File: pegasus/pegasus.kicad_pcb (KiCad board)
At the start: 2 copper layers, 50 x 120 mm, 15 parts, among them IC1 RFD900, IC2 Adafruit, IC3 Adafruit-BNO055-PCB, IC4 L70B-M39, IC5 L7805ACV, J1 Conn_01x02_Female, J2 Conn_01x02_Female, U1 Teensy4.1, U2 CON-SMA-EDGE-S, U3 CON-SMA-EDGE-S

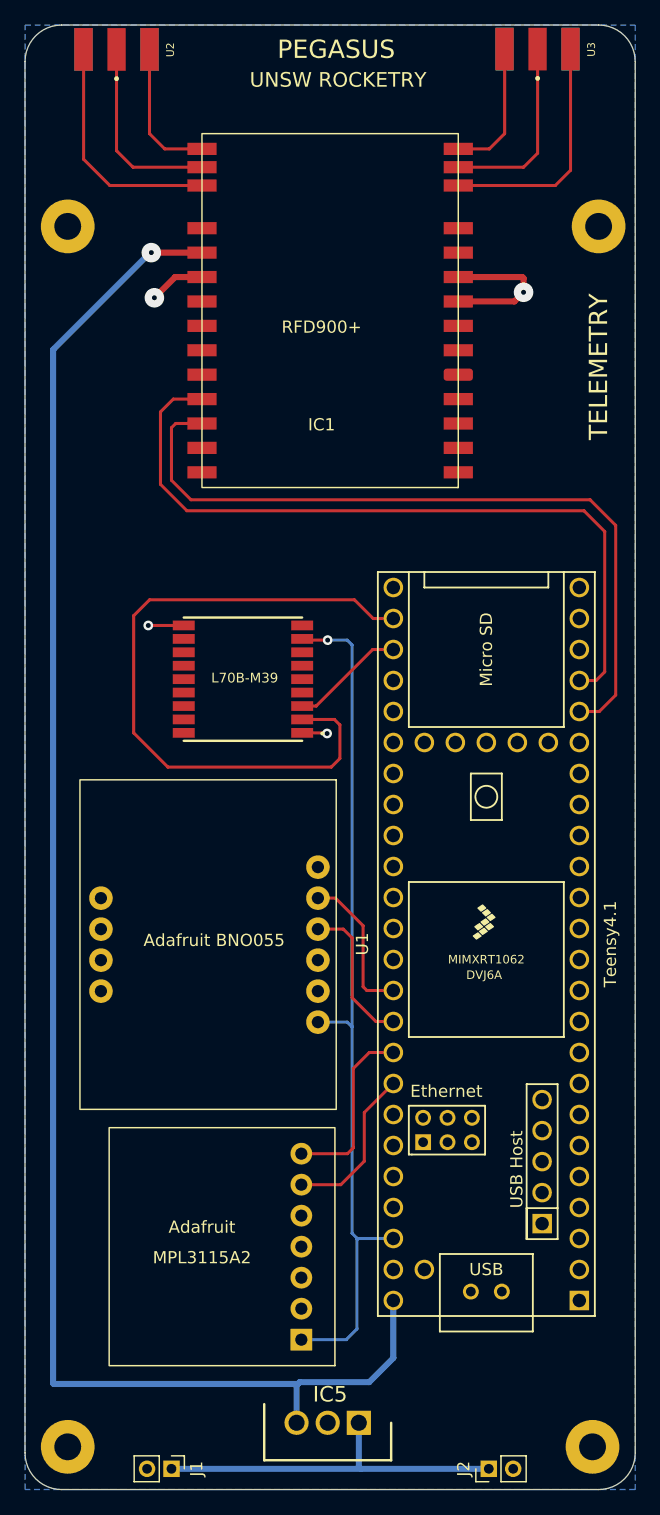
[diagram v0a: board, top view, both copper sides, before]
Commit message: added no connection flag to schematics, fixed minor mistakes on PCB and in footprints
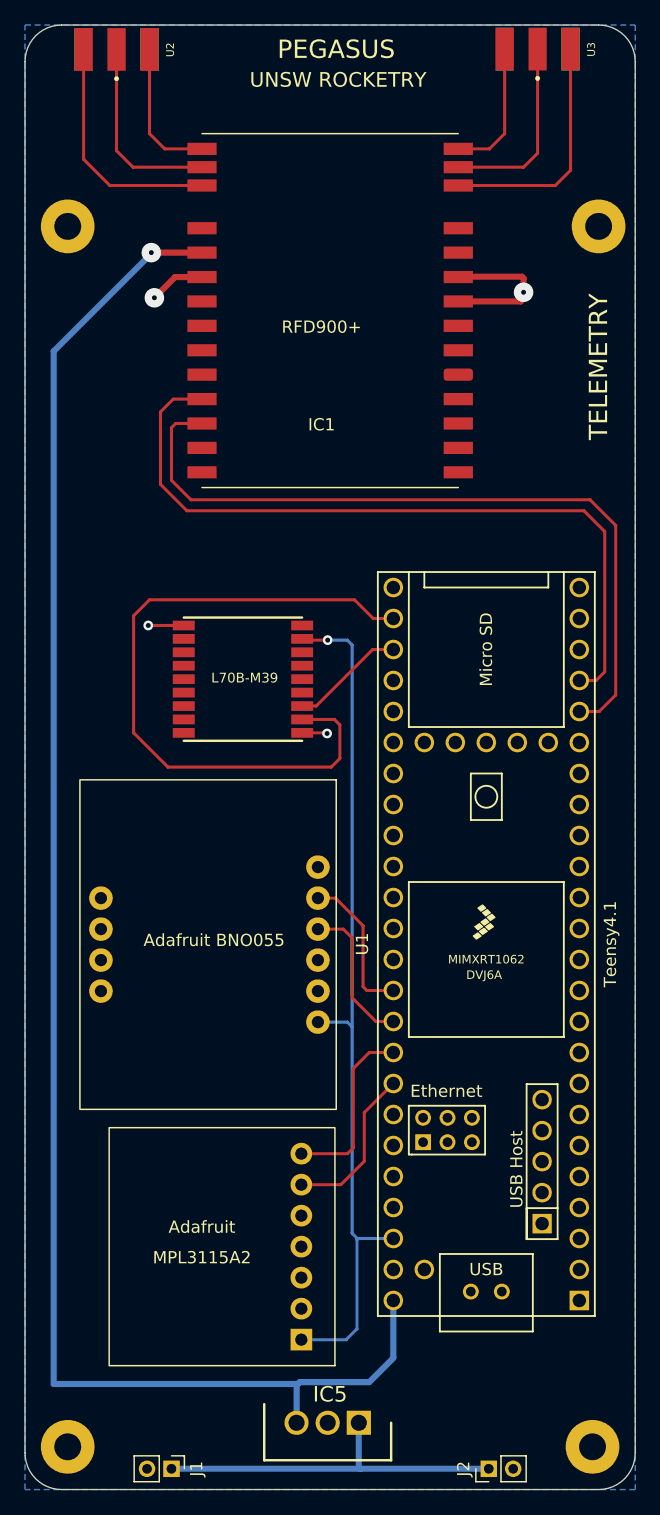
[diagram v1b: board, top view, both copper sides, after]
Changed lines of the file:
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@@
       (effects (font (size 1.27 1.27) (thickness 0.254)))
     )
-    (fp_line (start -4.85 -5.05) (end 4.85 -5.05) (layer "F.SilkS") (width 0.2))
     (fp_line (start 4.85 5.05) (end -4.85 5.05) (layer "F.SilkS") (width 0.2))
-    (fp_circle (center -6.502 -4.45) (end -6.502 -4.388) (layer "F.SilkS") (width 0.2) (fill none))
-    (fp_line (start -4.85 5.05) (end -4.85 -5.05) (layer "F.Fab") (width 0.2))
+    (fp_line (start -4.85 -5.05) (end 4.85 -5.05) (layer "F.SilkS") (width 0.2))
     (fp_line (start 4.85 -5.05) (end 4.85 5.05) (layer "F.Fab") (width 0.2))
-    (fp_line (start -4.85 -5.05) (end 4.85 -5.05) (layer "F.Fab") (width 0.2))
     (fp_line (start 4.85 5.05) (end -4.85 5.05) (layer "F.Fab") (width 0.2))
+    (fp_line (start -4.85 5.05) (end -4.85 -5.05) (layer "F.Fab") (width 0.2))
+    (fp_line (start -4.85 -5.05) (end 4.85 -5.05) (layer "F.Fab") (width 0.2))
     (pad "1" smd rect (at -4.85 -4.4 270) (size 0.8 1.8) (layers "F.Cu" "F.Paste" "F.Mask")
       (net 2 "GND") (pinfunction "GND_1") (pintype "passive"))
@@
       (effects (font (size 1 1) (thickness 0.15)))
     )
-    (fp_rect (start -6 -11.25) (end 15 17.75) (layer "F.SilkS") (width 0.12) (fill none))
+    (fp_line (start -6 -11.25) (end 15 -11.25) (layer "F.SilkS") (width 0.12))
+    (fp_line (start 15 17.75) (end -6 17.75) (layer "F.SilkS") (width 0.12))
+    (fp_line (start 15 -11.25) (end 15 17.75) (layer "Dwgs.User") (width 0.12))
+    (fp_line (start -6 17.75) (end -6 -11.25) (layer "Dwgs.User") (width 0.12))
     (pad "1" smd rect (at -6 -10 180) (size 2.4 1) (layers "F.Cu" "F.Paste" "F.Mask")
       (net 1 "unconnected-(IC1-Pad1)") (pinfunction "VUSB_5V") (pintype "input"))
@@
     (pad "28" smd rect (at 15 -10 180) (size 2.4 1) (layers "F.Cu" "F.Paste" "F.Mask")
       (net 24 "unconnected-(IC1-Pad28)") (pinfunction "CTS") (pintype "input"))
-    (group "" (id 5d567197-105f-4ed3-a4d4-dfc5e32b2ccc)
+    (group "" (id ccf65e24-b980-469f-8862-e397985c8f5a)
       (members
-        1bda36f6-3944-4bdf-b224-5bfc97f22460
-        25f77a41-6639-47ca-88a6-aa38a4b331a1
-        93e5cccc-95f5-49e8-be9b-0aba27195b61
-        b404786f-6892-43d8-8cbe-df439968c1ea
-        da67685b-35ec-44e4-9884-b9158b872c0e
-        de8f9472-fcc7-403f-a0e1-fee3a16774bd
+        01478f52-711e-460d-9130-927d9df325cb
+        142e2cf6-b82f-4007-9894-377d26b8ab0d
+        28221cea-e5dd-4443-909d-f89dc42a5054
+        59fe4e68-4119-4952-b511-7d1576b16691
+        7bdee640-e6be-4899-b318-a0ad1af68164
+        d9a88a97-e7e1-4571-8028-07e1b736766b
       )
     )
@@
     (fp_line (start -7.62 -0.635) (end -7.62 0.635) (layer "F.Fab") (width 0.2032))
     (fp_poly (pts
+        (xy -4.064 0.254)
+        (xy -3.556 0.254)
+        (xy -3.556 -0.254)
+        (xy -4.064 -0.254)
+      ) (layer "F.Fab") (width 0) (fill solid))
+    (fp_poly (pts
         (xy 3.556 0.254)
         (xy 4.064 0.254)
@@
       ) (layer "F.Fab") (width 0) (fill solid))
     (fp_poly (pts
-        (xy 3.556 -17.526)
-        (xy 4.064 -17.526)
-        (xy 4.064 -18.034)
-        (xy 3.556 -18.034)
-      ) (layer "F.Fab") (width 0) (fill solid))
-    (fp_poly (pts
-        (xy -1.524 0.254)
-        (xy -1.016 0.254)
-        (xy -1.016 -0.254)
-        (xy -1.524 -0.254)
-      ) (layer "F.Fab") (width 0) (fill solid))
-    (fp_poly (pts
         (xy -4.064 -17.526)
         (xy -3.556 -17.526)
@@
       ) (layer "F.Fab") (width 0) (fill solid))
     (fp_poly (pts
+        (xy -1.524 0.254)
+        (xy -1.016 0.254)
+        (xy -1.016 -0.254)
+        (xy -1.524 -0.254)
+      ) (layer "F.Fab") (width 0) (fill solid))
+    (fp_poly (pts
+        (xy 3.556 -17.526)
+        (xy 4.064 -17.526)
+        (xy 4.064 -18.034)
+        (xy 3.556 -18.034)
+      ) (layer "F.Fab") (width 0) (fill solid))
+    (fp_poly (pts
         (xy -1.524 -17.526)
         (xy -1.016 -17.526)
@@
       ) (layer "F.Fab") (width 0) (fill solid))
     (fp_poly (pts
-        (xy 1.016 0.254)
-        (xy 1.524 0.254)
-        (xy 1.524 -0.254)
-        (xy 1.016 -0.254)
-      ) (layer "F.Fab") (width 0) (fill solid))
-    (fp_poly (pts
-        (xy -4.064 0.254)
-        (xy -3.556 0.254)
-        (xy -3.556 -0.254)
-        (xy -4.064 -0.254)
-      ) (layer "F.Fab") (width 0) (fill solid))
-    (fp_poly (pts
         (xy 1.016 -17.526)
         (xy 1.524 -17.526)
@@
         (xy 1.016 -18.034)
       ) (layer "F.Fab") (width 0) (fill solid))
+    (fp_poly (pts
+        (xy 1.016 0.254)
+        (xy 1.524 0.254)
+        (xy 1.524 -0.254)
+        (xy 1.016 -0.254)
+      ) (layer "F.Fab") (width 0) (fill solid))
     (pad "1" thru_hole circle (at -6.35 0 180) (size 1.9304 1.9304) (drill 1) (layers *.Cu *.Mask)
       (net 101 "/+3.3V") (pinfunction "Vin_5V") (pintype "power_in") (solder_mask_margin 0.0508))
@@
     (pad "5" thru_hole circle (at 3.81 0 180) (size 1.9304 1.9304) (drill 1) (layers *.Cu *.Mask)
       (net 105 "/SCL1") (pinfunction "SCL-5V") (pintype "bidirectional") (solder_mask_margin 0.0508))
-    (pad "6" thru_hole circle (at 1.27 -17.78 180) (size 1.9304 1.9304) (drill 1) (layers *.Cu *.Mask)
-      (net 16 "unconnected-(IC3-Pad6)") (pinfunction "RST_5V") (pintype "bidirectional") (solder_mask_margin 0.0508))
     (pad "6" thru_hole circle (at 6.35 0 180) (size 1.9304 1.9304) (drill 1) (layers *.Cu *.Mask)
       (net 16 "unconnected-(IC3-Pad6)") (pinfunction "RST_5V") (pintype "bidirectional") (solder_mask_margin 0.0508))
+    (pad "6" thru_hole circle (at 1.27 -17.78 180) (size 1.9304 1.9304) (drill 1) (layers *.Cu *.Mask)
+      (net 16 "unconnected-(IC3-Pad6)") (pinfunction "RST_5V") (pintype "bidirectional") (solder_mask_margin 0.0508))
     (pad "7" thru_hole circle (at 3.81 -17.78 180) (size 1.9304 1.9304) (drill 1) (layers *.Cu *.Mask)
       (net 17 "unconnected-(IC3-Pad7)") (pinfunction "I2CAddr_3V") (pintype "bidirectional") (solder_mask_margin 0.0508))
@@
   )
   (segment (start 104.7 98) (end 104.75 98.05) (width 0.25) (layer "F.Cu") (net 2))
+  (segment (start 115.5 62.65) (end 120.62 62.65) (width 0.5) (layer "F.Cu") (net 2))
+  (segment (start 120.62 62.65) (end 120.85 62.42) (width 0.5) (layer "F.Cu") (net 2))
   (segment (start 90.1 89.2) (end 93.007 89.2) (width 0.25) (layer "F.Cu") (net 2))
-  (segment (start 115.5 60.65) (end 120.75 60.65) (width 0.5) (layer "F.Cu") (net 2))
+  (segment (start 115.53 60.62) (end 120.72 60.62) (width 0.5) (layer "F.Cu") (net 2))
   (segment (start 92.3 60.65) (end 90.6 62.35) (width 0.5) (layer "F.Cu") (net 2))
-  (segment (start 120.75 60.65) (end 120.85 60.75) (width 0.5) (layer "F.Cu") (net 2))
-  (segment (start 102.707 98) (end 104.7 98) (width 0.25) (layer "F.Cu") (net 2))
-  (segment (start 120.1 62.65) (end 120.85 61.9) (width 0.5) (layer "F.Cu") (net 2))
   (segment (start 120.85 60.75) (end 120.85 61.9) (width 0.5) (layer "F.Cu") (net 2))
-  (segment (start 115.5 62.65) (end 120.1 62.65) (width 0.5) (layer "F.Cu") (net 2))
+  (segment (start 120.72 60.62) (end 120.85 60.75) (width 0.5) (layer "F.Cu") (net 2))
+  (segment (start 120.85 62.42) (end 120.85 61.9) (width 0.5) (layer "F.Cu") (net 2))
+  (segment (start 102.707 98) (end 104.7 98) (width 0.25) (layer "F.Cu") (net 2))
+  (segment (start 115.5 60.65) (end 115.53 60.62) (width 0.5) (layer "F.Cu") (net 2))
   (segment (start 94.5 60.65) (end 92.3 60.65) (width 0.5) (layer "F.Cu") (net 2))
   (via (at 90.6 62.35) (size 1.6) (drill 0.4) (layers "F.Cu" "B.Cu") (net 2))
@@
   (segment (start 119.3 48.9) (end 119.3 41.9725) (width 0.25) (layer "F.Cu") (net 12))
   (segment (start 115.5 50.15) (end 118.05 50.15) (width 0.25) (layer "F.Cu") (net 12))
-  (segment (start 90.4 40.6275) (end 90.44 40.5875) (width 0.25) (layer "F.Cu") (net 13))
   (segment (start 91.45 50.15) (end 90.2 48.9) (width 0.25) (layer "F.Cu") (net 13))
   (segment (start 94.5 50.15) (end 91.45 50.15) (width 0.25) (layer "F.Cu") (net 13))
@@
   (segment (start 90.35 58.65) (end 94.5 58.65) (width 0.5) (layer "F.Cu") (net 106))
   (via (at 90.35 58.65) (size 1.6) (drill 0.4) (layers "F.Cu" "B.Cu") (net 106))
-  (segment (start 102.35 151.35) (end 82.35 151.35) (width 0.5) (layer "B.Cu") (net 106))
   (segment (start 110.18 149.22) (end 110.18 144.51) (width 0.5) (layer "B.Cu") (net 106))
-  (segment (start 82.35 151.35) (end 82.3 151.3) (width 0.5) (layer "B.Cu") (net 106))
   (segment (start 102.25 151.45) (end 102.5 151.2) (width 0.25) (layer "B.Cu") (net 106))
-  (segment (start 82.3 151.3) (end 82.3 66.6) (width 0.5) (layer "B.Cu") (net 106))
+  (segment (start 102.35 151.35) (end 82.35 151.35) (width 0.5) (layer "B.Cu") (net 106))
   (segment (start 102.25 154.53) (end 102.25 151.45) (width 0.5) (layer "B.Cu") (net 106))
   (segment (start 102.5 151.2) (end 102.35 151.35) (width 0.5) (layer "B.Cu") (net 106))
+  (segment (start 90.25 58.83) (end 90.25 58.65) (width 0.5) (layer "B.Cu") (net 106))
   (segment (start 108.2 151.2) (end 110.18 149.22) (width 0.5) (layer "B.Cu") (net 106))
-  (segment (start 82.4 151.2) (end 82.3 151.3) (width 0.25) (layer "B.Cu") (net 106))
+  (segment (start 82.35 151.35) (end 82.35 66.73) (width 0.5) (layer "B.Cu") (net 106))
+  (segment (start 82.35 66.73) (end 90.25 58.83) (width 0.5) (layer "B.Cu") (net 106))
   (segment (start 102.5 151.2) (end 108.2 151.2) (width 0.5) (layer "B.Cu") (net 106))
-  (segment (start 82.3 66.6) (end 90.25 58.65) (width 0.5) (layer "B.Cu") (net 106))
   (zone (net 2) (net_name "GND") (layer "B.Cu") (name "Ground Plane") (hatch edge 0.508)
     (priority 3)

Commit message: fixed BNO055 pin numbering, cleaned up schematic
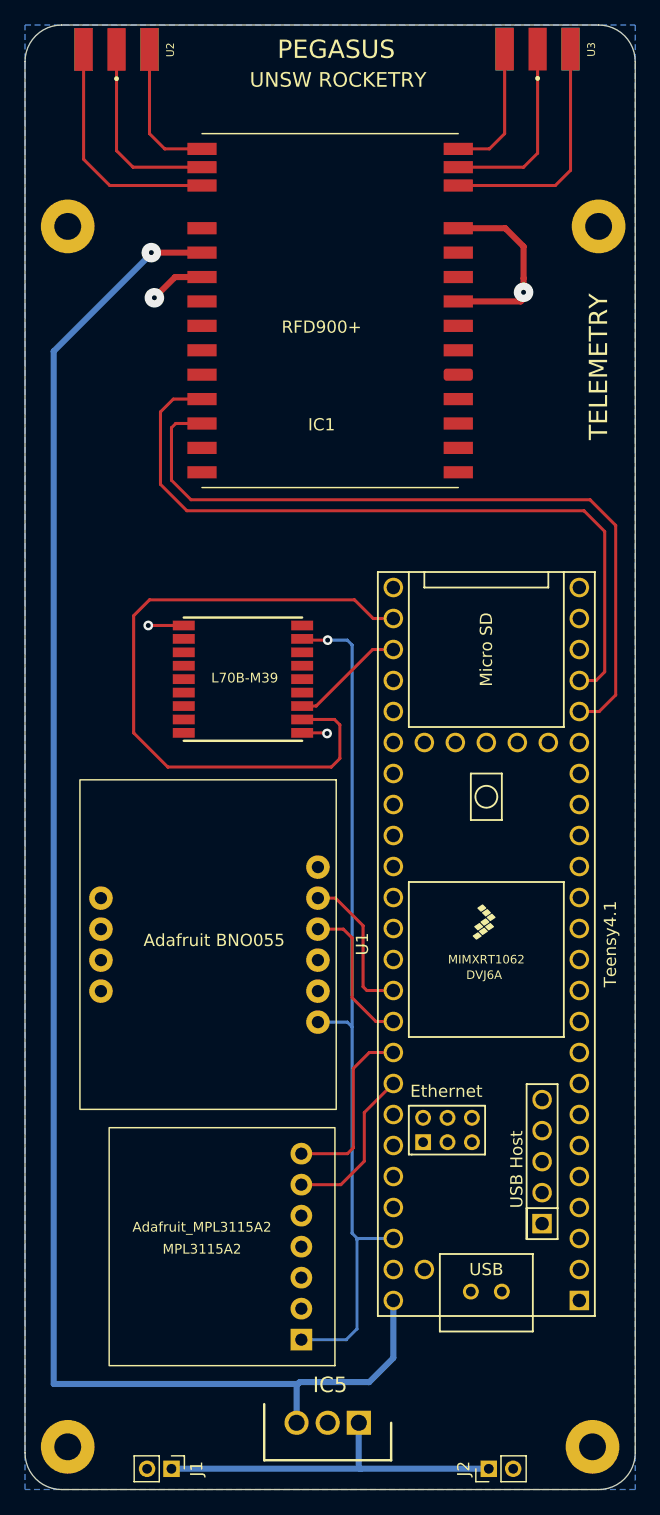
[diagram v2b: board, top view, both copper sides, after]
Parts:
- IC2: value Adafruit -> Adafruit_MPL3115A2
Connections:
- net 3.7V renamed +3.7V
- IC1 pad 9: GND -> unconnected-(IC1-Pad9)
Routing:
- net GND: track 22.1 -> 25.3 mm
